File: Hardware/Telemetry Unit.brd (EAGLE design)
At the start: 50.8 x 63.5 mm, 56 parts, among them IC1 MEGA128-A, IC2 FT232RL, J2 503182-1852, J3 10118193-0001LF, Q1 10MHz, U1 MPL3115A2, U2 AOZ1280, U3 LSM6DS3

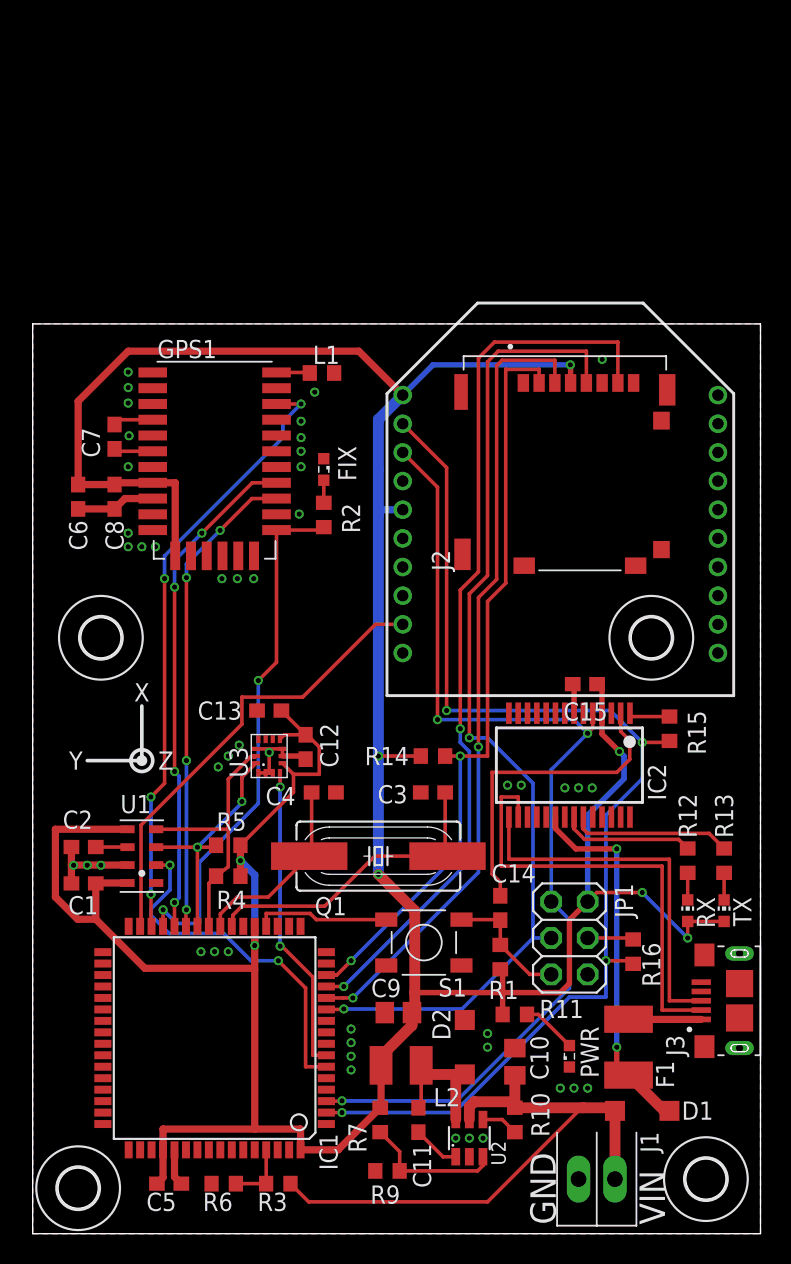
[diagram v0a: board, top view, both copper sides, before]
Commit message: Larger board, fix GPS/SD placement
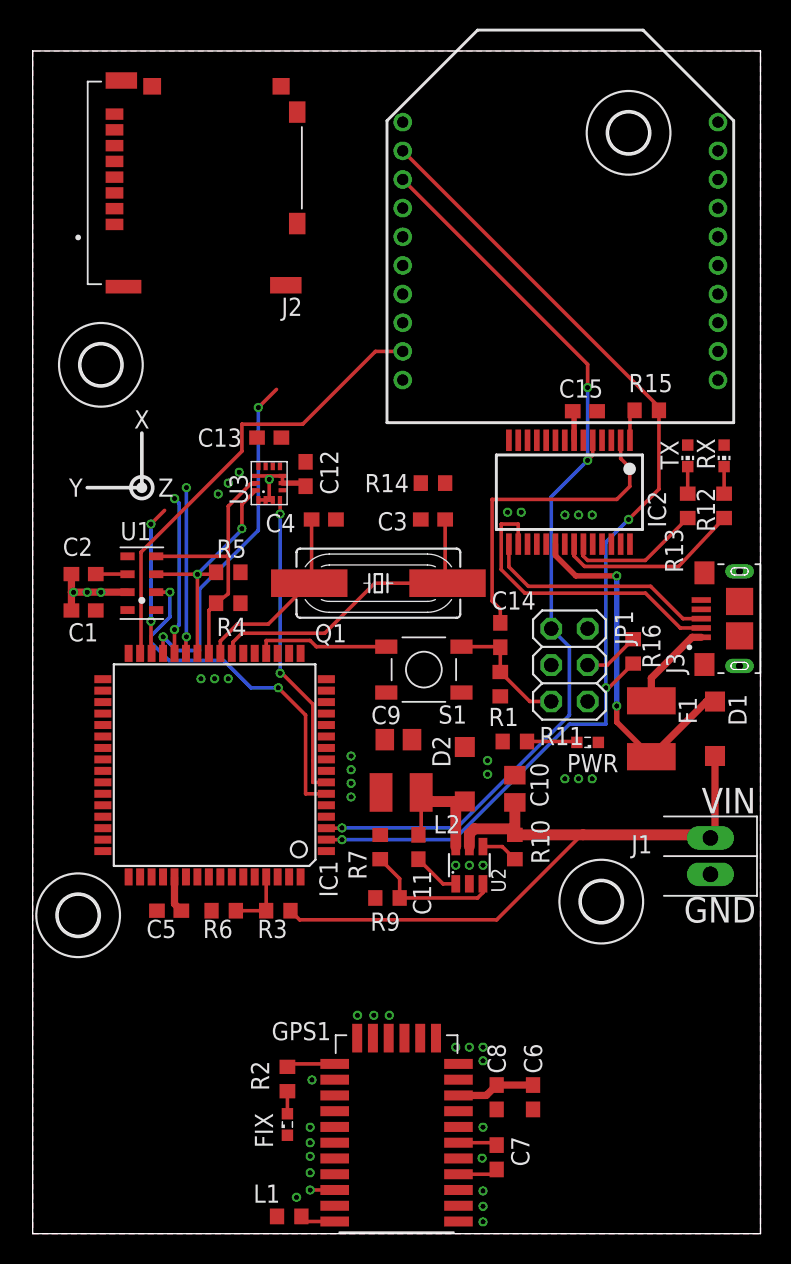
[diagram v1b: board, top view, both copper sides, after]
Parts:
- moved L1 58.9 mm to (17.9, 1.21), turned to 180 degrees
- moved C7 56.9 mm to (32.4, 5.33), turned to 90 degrees
- moved C6 52.6 mm to (34.9, 9.53), turned to 90 degrees
- moved GPS1 49.9 mm to (25.4, 6.35), turned to 180 degrees
- moved C8 49.7 mm to (32.4, 9.53), turned to 90 degrees
- moved FIX 45.8 mm to (17.8, 7.62), turned to 90 degrees
- moved R2 39.5 mm to (17.8, 10.8), turned to 270 degrees
- moved U$3 35.3 mm to (41.6, 76.8)
- moved J2 32.3 mm to (12.1, 73.3), turned to 90 degrees
- moved RX 31.9 mm to (48.3, 54.3), turned to 180 degrees
- moved TX 31.9 mm to (45.7, 54.3), turned to 180 degrees
- moved D1 27.1 mm to (47.6, 35.2), turned to 90 degrees
- moved J3 26.7 mm to (49.3, 42.9)
- moved R12 24.9 mm to (48.3, 50.8), turned to 270 degrees
- moved R13 24.9 mm to (45.7, 50.8), turned to 270 degrees
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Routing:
- net +3V3: track 256.4 -> 0.00 mm, vias 8 -> 0
- net SCK: track 70.5 -> 0.00 mm, vias 2 -> 0
- net MISO: track 62.5 -> 0.00 mm, vias 2 -> 0
- net MOSI: track 55.9 -> 0.00 mm, vias 2 -> 0
- net CS_SD: track 53.3 -> 0.00 mm, vias 2 -> 0
- net !GPS_SLP: track 42.6 -> 12.1 mm, vias 4 -> 3
- net TX1: track 35.2 -> 11.1 mm, vias 4 -> 2
- net RX1: track 33.5 -> 11.6 mm, vias 4 -> 2
- net N$11: track 31.4 -> 21.4 mm
- net N$13: track 26.2 -> 16.5 mm
- net FIX: track 37.3 -> 28.1 mm
- net VBAT: track 42.1 -> 49.2 mm
- net RX0/PDI: track 81.5 -> 74.4 mm, vias 4 -> 3
- net TX0/PDO: track 71.7 -> 66.1 mm
- net N$18: track 9.33 -> 13.1 mm
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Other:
- board size 50.8 x 63.5 mm -> 50.8 x 82.5 mm

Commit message: Wide-Range Accelerometer
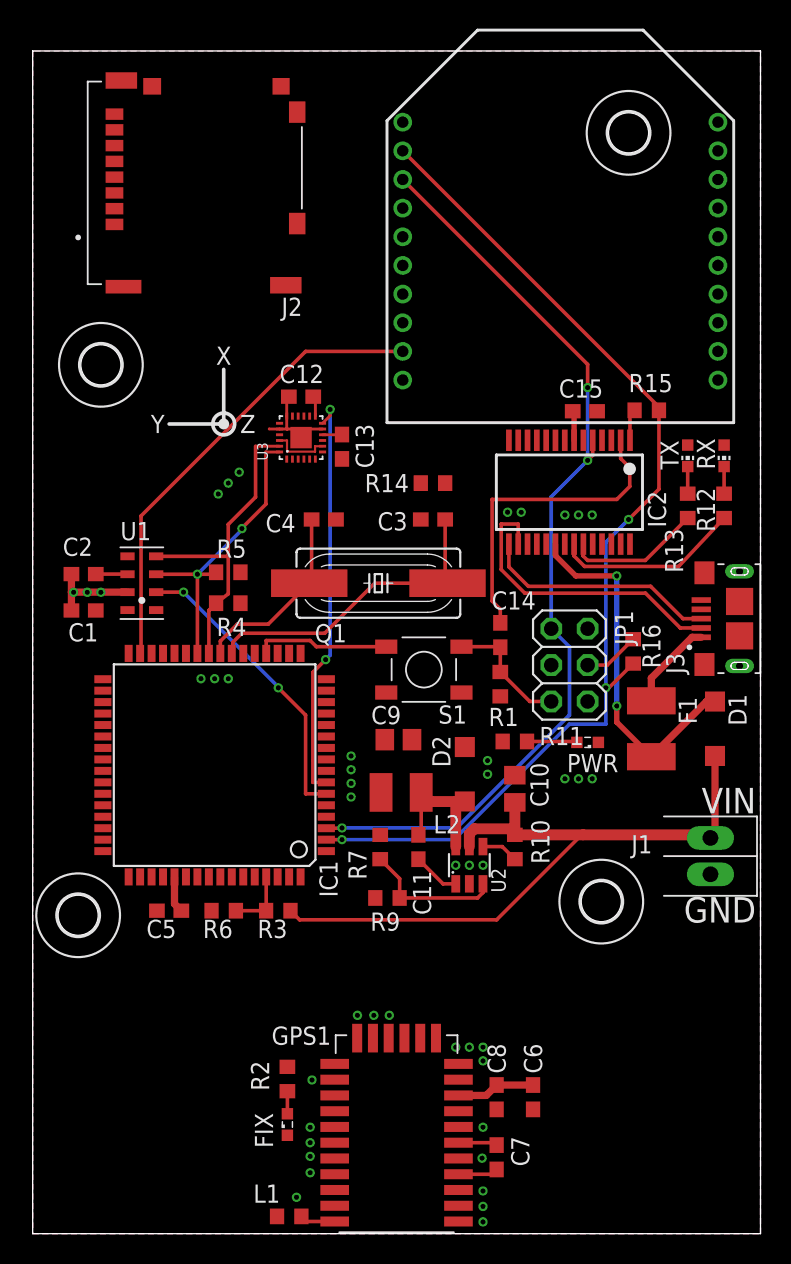
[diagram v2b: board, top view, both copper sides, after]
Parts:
- C13: value 2.2u -> 100n
- U3: value LSM6DS3 -> ICM-20649; device TrackerPeripherals:14-LGA -> TrackerPeripherals:QFN24-3X3
- moved C12 5.41 mm to (18.7, 58.4), turned to 180 degrees
- moved C13 5.12 mm to (21.6, 54.9), turned to 270 degrees
- moved U3 3.88 mm to (18.7, 55.6)
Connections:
- new net N$8: C13.1, U3.10
- net +3V3: now also U3.13, U3.22; no longer C13.1, U3.5
- net ACCEL_INT: now also U3.12; no longer U3.4
- net GND: now also U3.11, U3.18, U3.20, U3.9, U3.EXP; no longer U3.1, U3.12, U3.2, U3.3, U3.6, U3.7
- net SCL: now also U3.23; no longer U3.13
- net SDA: now also U3.24; no longer U3.14
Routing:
- net FIX: track 28.1 -> 0.00 mm, vias 2 -> 0
- net !GPS_SLP: track 12.1 -> 0.00 mm, vias 3 -> 0
- net RX1: track 11.6 -> 0.00 mm, vias 2 -> 0
- net TX1: track 11.1 -> 0.00 mm, vias 2 -> 0
- net ACCEL_INT: track 21.7 -> 28.7 mm
- net +3V3: track 0.00 -> 5.66 mm
- net SCL: track 18.5 -> 22.6 mm
- net SDA: track 17.6 -> 21.5 mm
- net ALT_INT: track 24.9 -> 21.0 mm
- net N$8: track 0.00 -> 1.37 mm
- net GND: track 24.2 -> 23.7 mm, vias 45 -> 44

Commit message: Re-route power
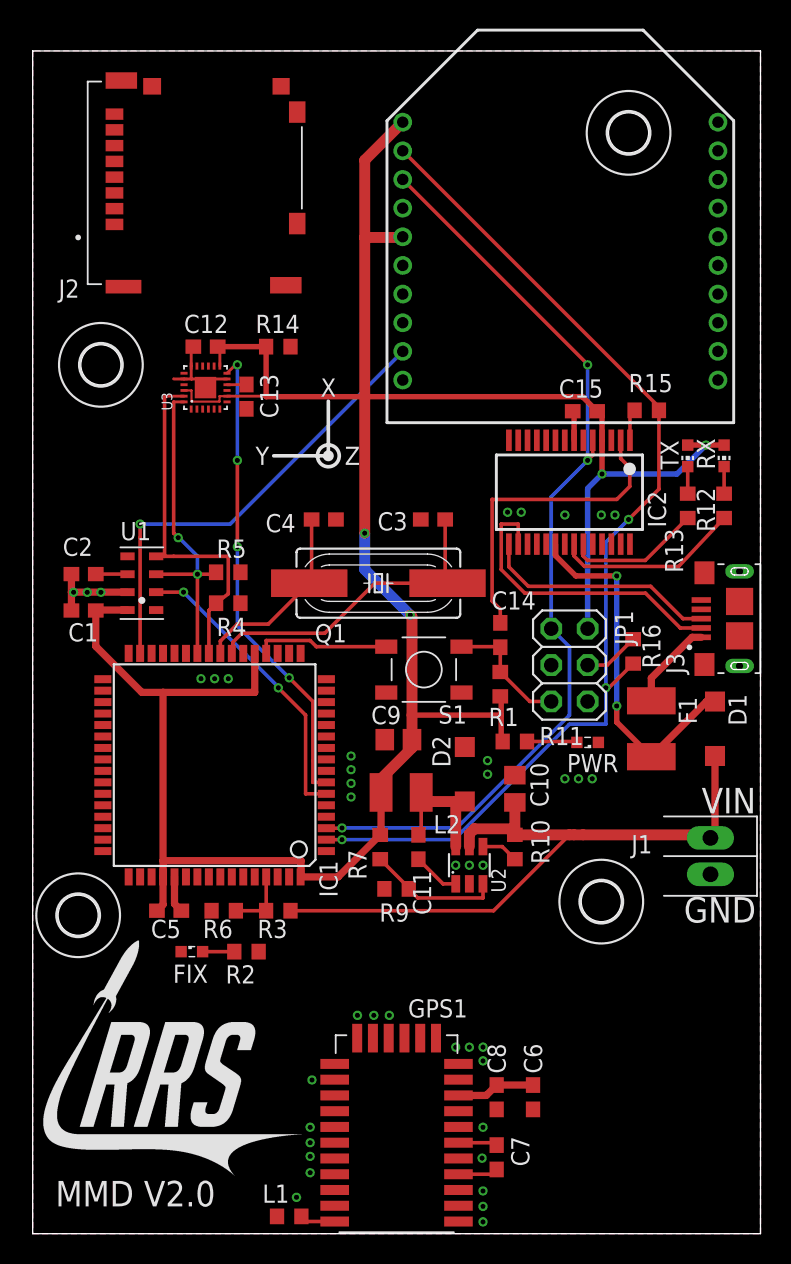
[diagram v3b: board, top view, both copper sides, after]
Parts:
- moved R14 14.4 mm to (17.1, 61.9)
- moved FIX 13.8 mm to (11.1, 19.7), turned to 0 degrees
- moved R2 9.34 mm to (14.9, 19.7), turned to 180 degrees
- moved C12 7.53 mm to (12.1, 61.9)
- moved U3 7.53 mm to (12.1, 59.1)
- moved C13 7.53 mm to (14.9, 58.4)
- moved R9 0.90 mm to (25.4, 24.1)
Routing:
- net +3V3: track 5.66 -> 183.1 mm, vias 0 -> 4
- net ACCEL_INT: track 28.7 -> 33.2 mm, vias 2 -> 4
- net SCL: track 22.6 -> 25.0 mm
- net SDA: track 21.5 -> 23.5 mm
- net VBAT: track 49.2 -> 47.7 mm
- net N$6: track 1.58 -> 2.21 mm
- net N$10: track 9.85 -> 9.33 mm
- net RF_SLP: track 32.6 -> 32.3 mm, vias 0 -> 1
- net GND: vias 44 -> 41
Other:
- board text added: "MMD V2.0"
- board text removed: "MMD V1.1"

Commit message: Reroute remianing signals and stitch grounds
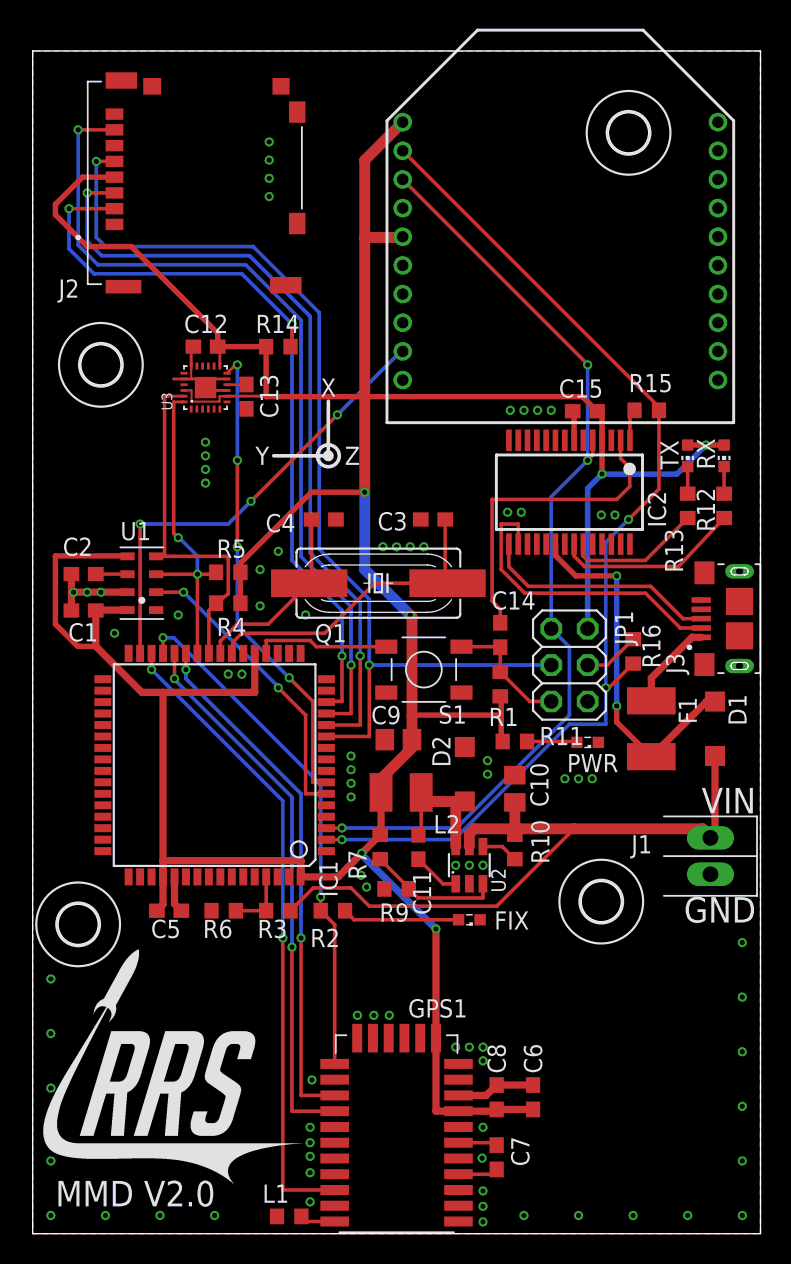
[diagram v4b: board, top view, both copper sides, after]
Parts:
- moved FIX 19.5 mm to (30.5, 21.9), turned to 180 degrees
- moved R2 6.68 mm to (21.0, 22.5), turned to 0 degrees
- moved U$4 0.64 mm to (3.17, 21.6)
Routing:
- net +3V3: track 183.1 -> 258.3 mm, vias 4 -> 6
- net SCK: track 0.00 -> 71.0 mm, vias 0 -> 2
- net MISO: track 0.00 -> 58.9 mm, vias 0 -> 2
- net MOSI: track 0.00 -> 55.3 mm, vias 0 -> 2
- net CS_SD: track 0.00 -> 54.3 mm, vias 0 -> 3
- net !GPS_SLP: track 0.00 -> 44.9 mm, vias 0 -> 2
- net TX1: track 0.00 -> 38.3 mm, vias 0 -> 2
- net RX1: track 0.00 -> 36.5 mm, vias 0 -> 2
- net FIX: track 0.00 -> 36.2 mm, vias 0 -> 2
- net N$6: track 2.21 -> 8.19 mm
- net VBAT: track 47.7 -> 49.7 mm
- net GND: track 23.7 -> 25.2 mm, vias 41 -> 81
- net RF_SLP: vias 1 -> 3
